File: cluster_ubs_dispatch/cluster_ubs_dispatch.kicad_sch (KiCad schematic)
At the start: 15 parts, among them J1 USB_A_external, J10 USB_A_jetson_NC, J11 Conn_01x08_Pin, J2 USB_A_ard_leo_pico, J3 USB_A_jetson_NC2, J4 USB_A_jetson0, J5 USB_A_jetson1, J6 USB_A_jetson2, J7 USB_A_jetson3, J8 USB_A_jetson4, J9 USB_A_jetson5, U1 74HC4051, U2 74HC4051, U3 74HC4051, U4 74HC4051

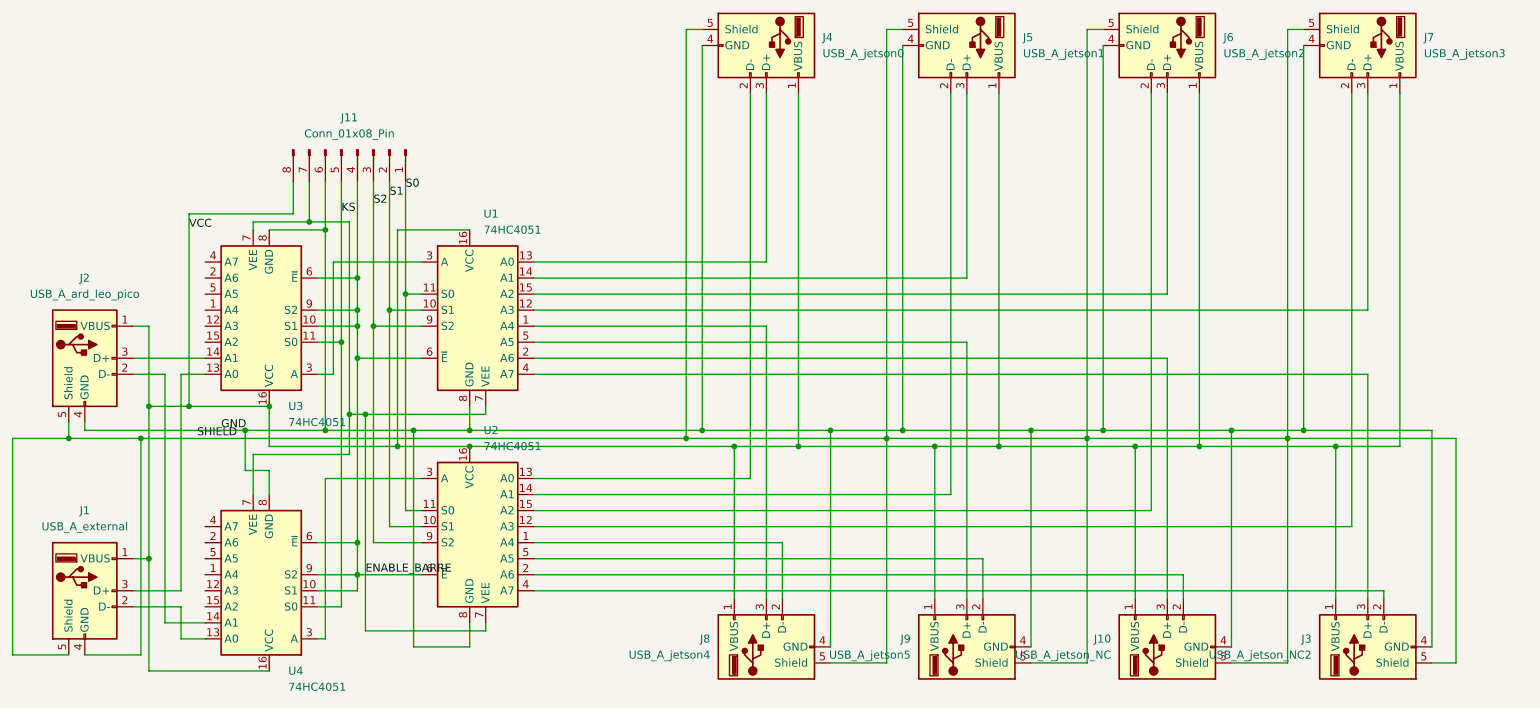
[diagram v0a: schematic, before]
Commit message: missing additional S connection
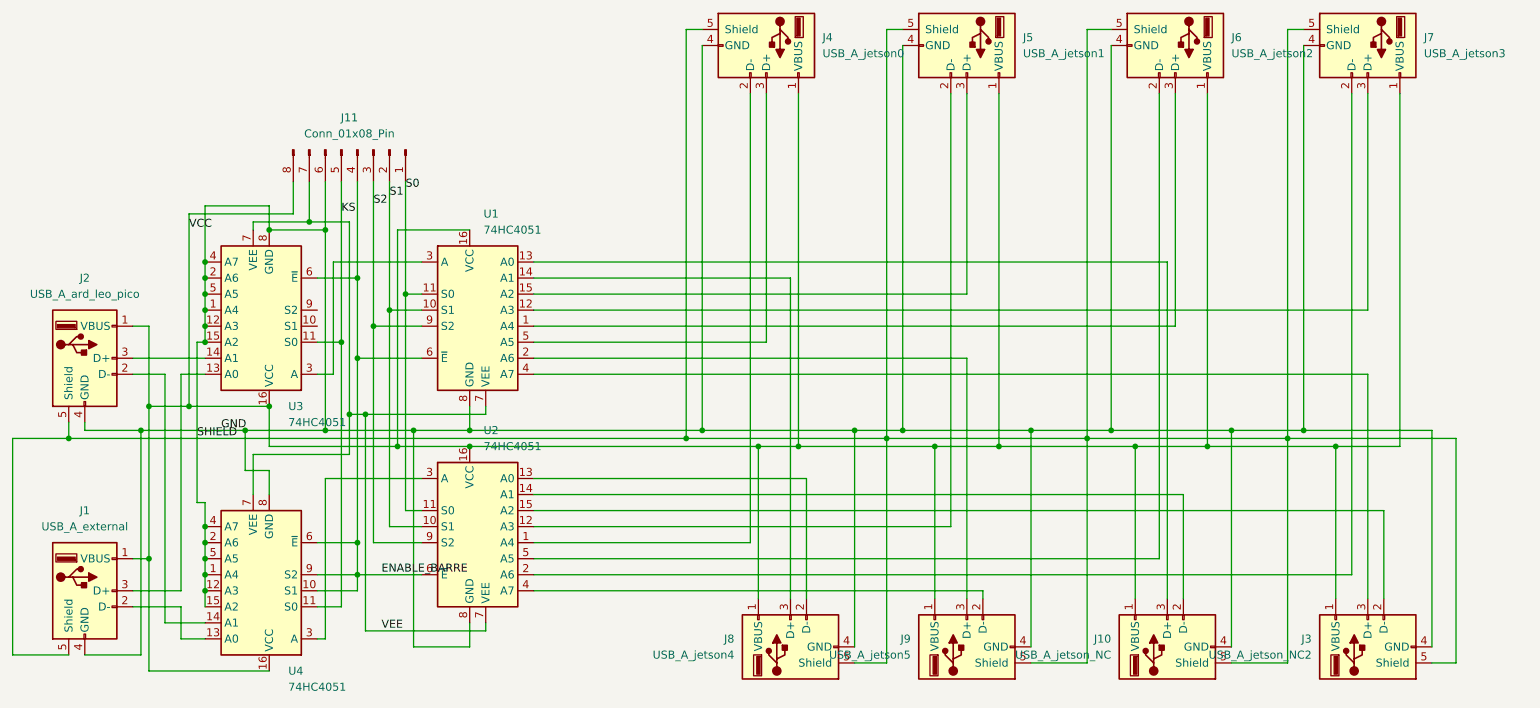
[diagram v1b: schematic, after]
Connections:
- net SHIELD is gone; now on net GND: J1.4 (GND), J1.5 (Shield), J10.5 (Shield), J2.5 (Shield), J3.5 (Shield), J4.5 (Shield), J5.5 (Shield), J6.5 (Shield), J7.5 (Shield), J8.5 (Shield), J9.5 (Shield)
- net ENABLE_BARRE: no longer J11.7 (Pin_7), U1.7 (VEE), U2.7 (VEE), U3.10 (S1), U3.7 (VEE), U3.9 (S2), U4.7 (VEE)
- net GND: now also U3.1 (A4), U3.12 (A3), U3.15 (A2), U3.2 (A6), U3.4 (A7), U3.5 (A5), U4.1 (A4), U4.12 (A3), U4.15 (A2), U4.2 (A6), U4.4 (A7), U4.5 (A5)
- net at U2.1 (A4): now also J4.2 (D-); no longer J8.2 (D-)
- net at U2.12 (A3): now also J5.2 (D-); no longer J7.2 (D-)
- net at U2.13 (A0): now also J8.2 (D-); no longer J4.2 (D-)
- net at U2.14 (A1): now also J10.2 (D-); no longer J5.2 (D-)
- net at U2.15 (A2): now also J3.2 (D-); no longer J6.2 (D-)
- net at U2.2 (A6): now also J7.2 (D-); no longer J10.2 (D-)
- net at U2.4 (A7): now also J9.2 (D-); no longer J3.2 (D-)
- net at U2.5 (A5): now also J6.2 (D-); no longer J9.2 (D-)
- net at J6.3 (D+): now also U1.1 (A4); no longer U1.15 (A2)
- net at J4.3 (D+): now also U1.5 (A5); no longer U1.13 (A0)
- net at J8.3 (D+): now also U1.14 (A1); no longer U1.1 (A4)
- net at J10.3 (D+): now also U1.13 (A0); no longer U1.2 (A6)
- net at J5.3 (D+): now also U1.15 (A2); no longer U1.14 (A1)
- net at J9.3 (D+): now also U1.2 (A6); no longer U1.5 (A5)
- new net VEE: J11.7 (Pin_7), U1.7 (VEE), U2.7 (VEE), U3.7 (VEE), U4.7 (VEE)
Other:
- moved on the sheet: J6, J8
